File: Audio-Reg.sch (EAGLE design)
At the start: 18 parts, among them IC1 3.3V, Q1 NPN2SC3422-2, Q2 NPN2SC3325, Q3 PNP2SA1313

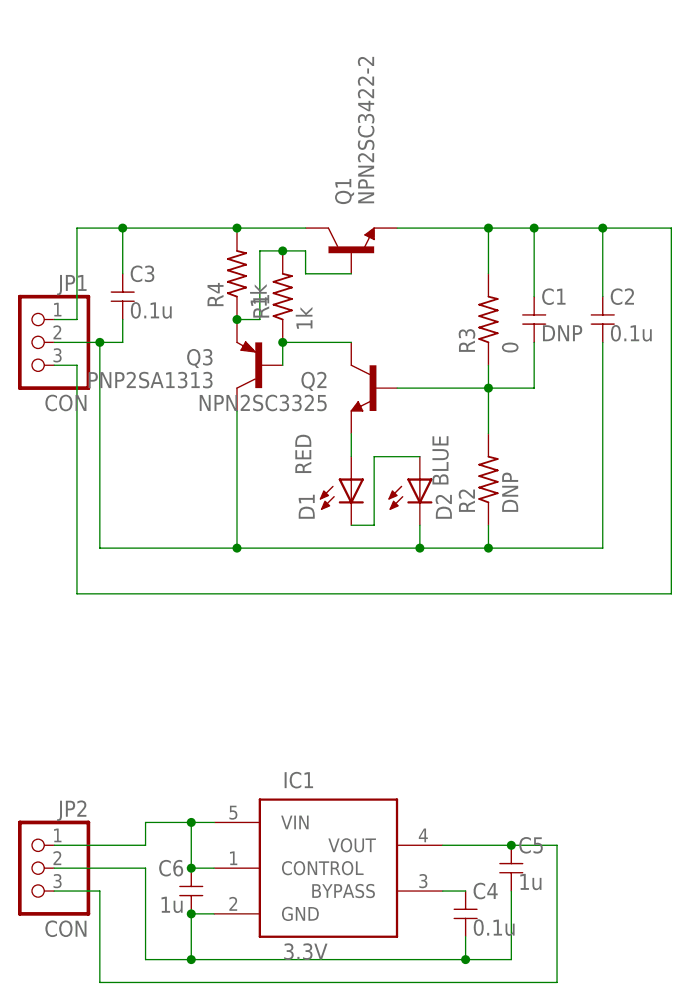
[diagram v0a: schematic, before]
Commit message: 回路図を修正
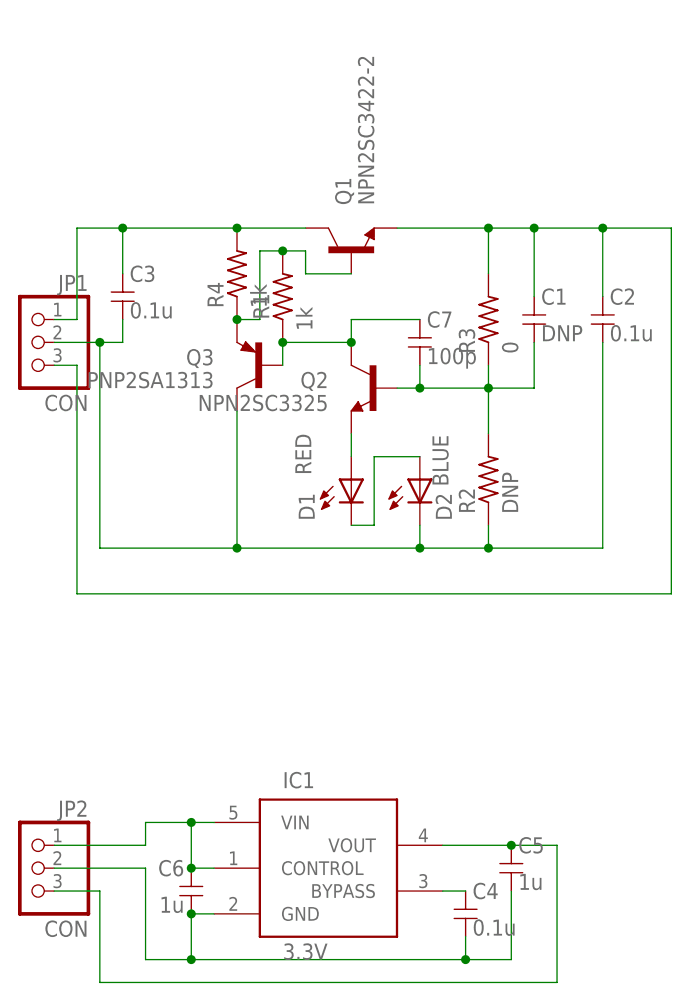
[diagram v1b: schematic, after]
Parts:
- added C7: 100p, my_rcl:C-1608
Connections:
- net N$10: now also C7.1
- net N$3: now also C7.2
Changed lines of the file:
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@@
 <?xml version="1.0" encoding="utf-8"?>
 <!DOCTYPE eagle SYSTEM "eagle.dtd">
-<eagle version="9.6.1">
+<eagle version="9.6.2">
 <drawing>
 <settings>
@@
 <part name="R1" library="my_rcl" deviceset="R" device="-1608" value="1k"/>
 <part name="R4" library="my_rcl" deviceset="R" device="-1608" value="1k"/>
+<part name="C7" library="my_rcl" deviceset="C" device="-1608" value="100p"/>
 </parts>
 <sheets>
@@
 <attribute name="NAME" x="1.0414" y="24.13" size="1.778" layer="95" rot="R90"/>
 <attribute name="VALUE" x="5.842" y="24.13" size="1.778" layer="96" rot="R90"/>
+</instance>
+<instance part="C7" gate="G$1" x="22.86" y="20.32" smashed="yes">
+<attribute name="NAME" x="23.622" y="21.971" size="1.778" layer="95"/>
+<attribute name="VALUE" x="23.622" y="17.907" size="1.778" layer="96"/>
 </instance>
 </instances>
@@
 <segment>
 <pinref part="Q2" gate="G$1" pin="B"/>
-<wire x1="20.32" y1="15.24" x2="30.48" y2="15.24" width="0.1524" layer="91"/>
+<wire x1="20.32" y1="15.24" x2="22.86" y2="15.24" width="0.1524" layer="91"/>
 <pinref part="R2" gate="G$1" pin="2"/>
+<wire x1="22.86" y1="15.24" x2="30.48" y2="15.24" width="0.1524" layer="91"/>
 <wire x1="30.48" y1="15.24" x2="30.48" y2="10.16" width="0.1524" layer="91"/>
 <pinref part="R3" gate="G$1" pin="1"/>
@@
 <pinref part="C1" gate="G$1" pin="2"/>
 <wire x1="35.56" y1="15.24" x2="35.56" y2="20.32" width="0.1524" layer="91"/>
+<pinref part="C7" gate="G$1" pin="2"/>
+<wire x1="22.86" y1="17.78" x2="22.86" y2="15.24" width="0.1524" layer="91"/>
+<junction x="22.86" y="15.24"/>
 </segment>
 </net>
@@
 <wire x1="7.62" y1="20.32" x2="15.24" y2="20.32" width="0.1524" layer="91"/>
 <junction x="7.62" y="20.32"/>
-</segment>
-</net>
+<pinref part="C7" gate="G$1" pin="1"/>
+<wire x1="22.86" y1="22.86" x2="15.24" y2="22.86" width="0.1524" layer="91"/>
+<wire x1="15.24" y1="22.86" x2="15.24" y2="20.32" width="0.1524" layer="91"/>
+<junction x="15.24" y="20.32"/>
+</segment>
+</net>
